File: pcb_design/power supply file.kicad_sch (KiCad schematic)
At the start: 6 parts, among them U3 L78M05CDT, U4 L78M05CDT

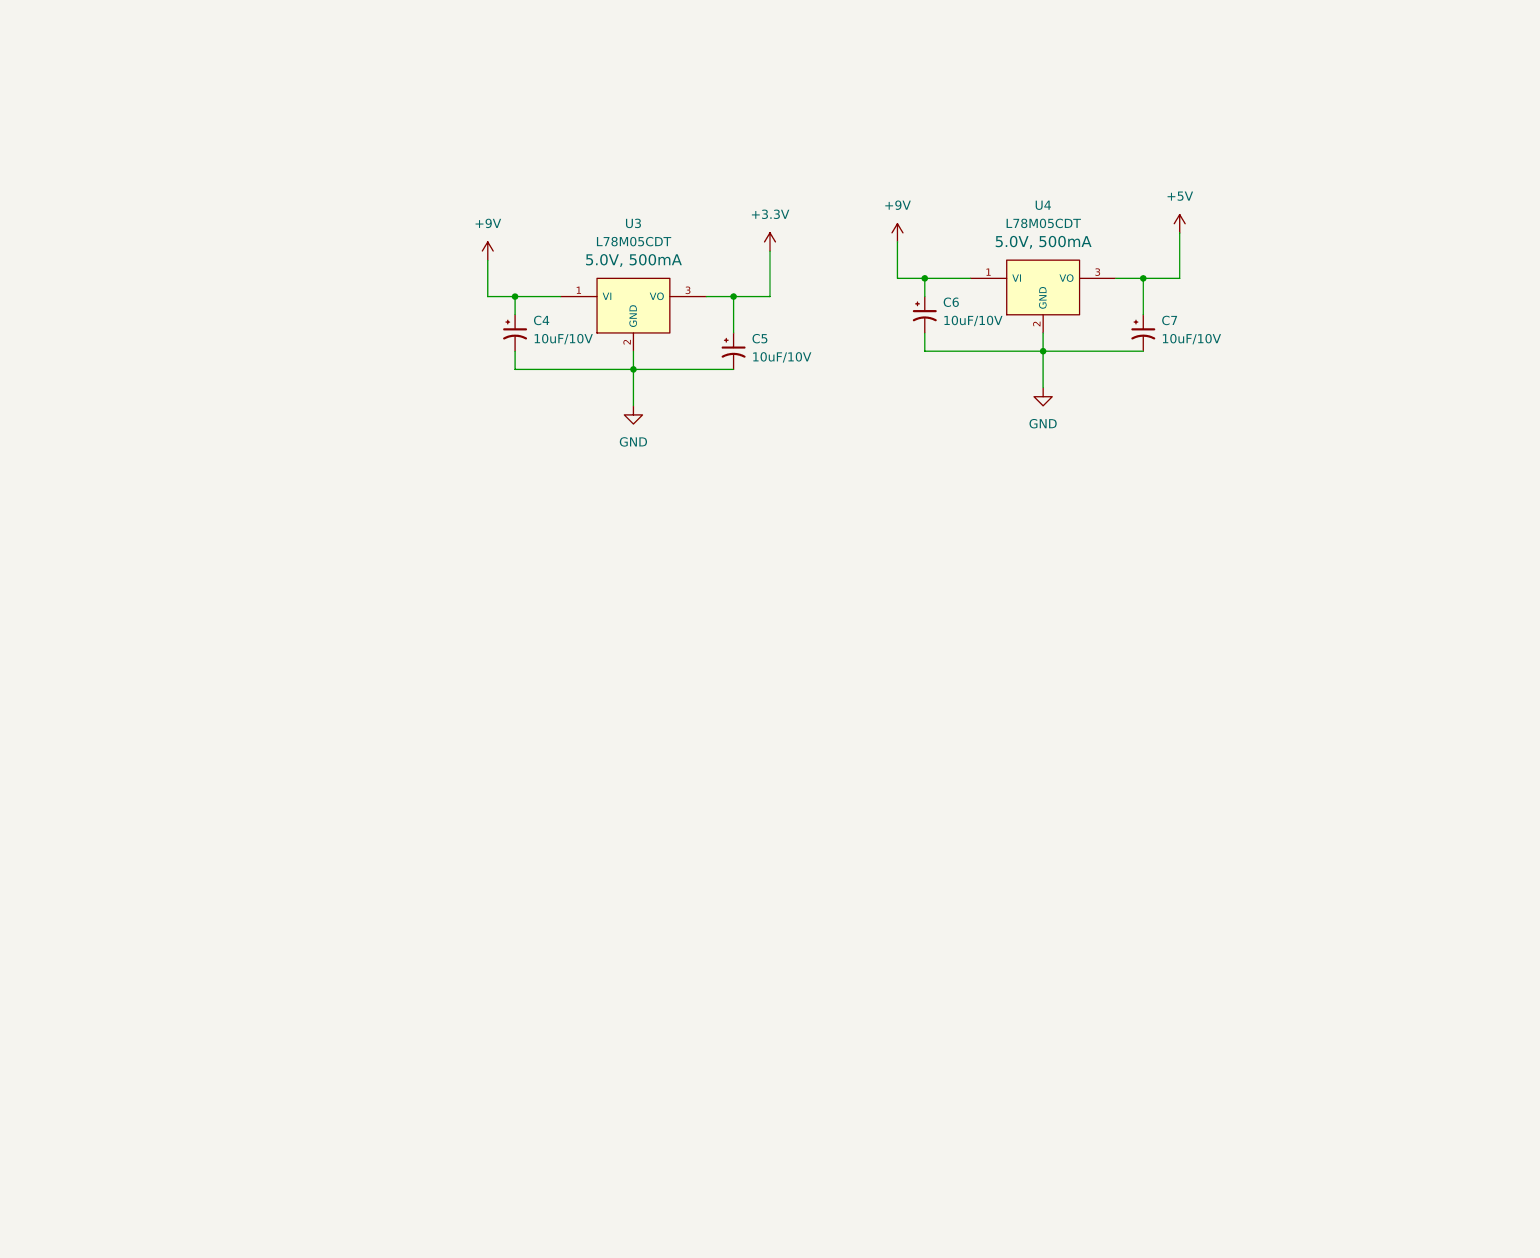
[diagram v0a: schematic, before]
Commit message: cambio de regulador de alto iq por reguladores de bajo iq separados uno para sensores y otro para micro y comunicacion usando el lt8610, apagado de alimentacion de sensores atravez de mosfet canal p
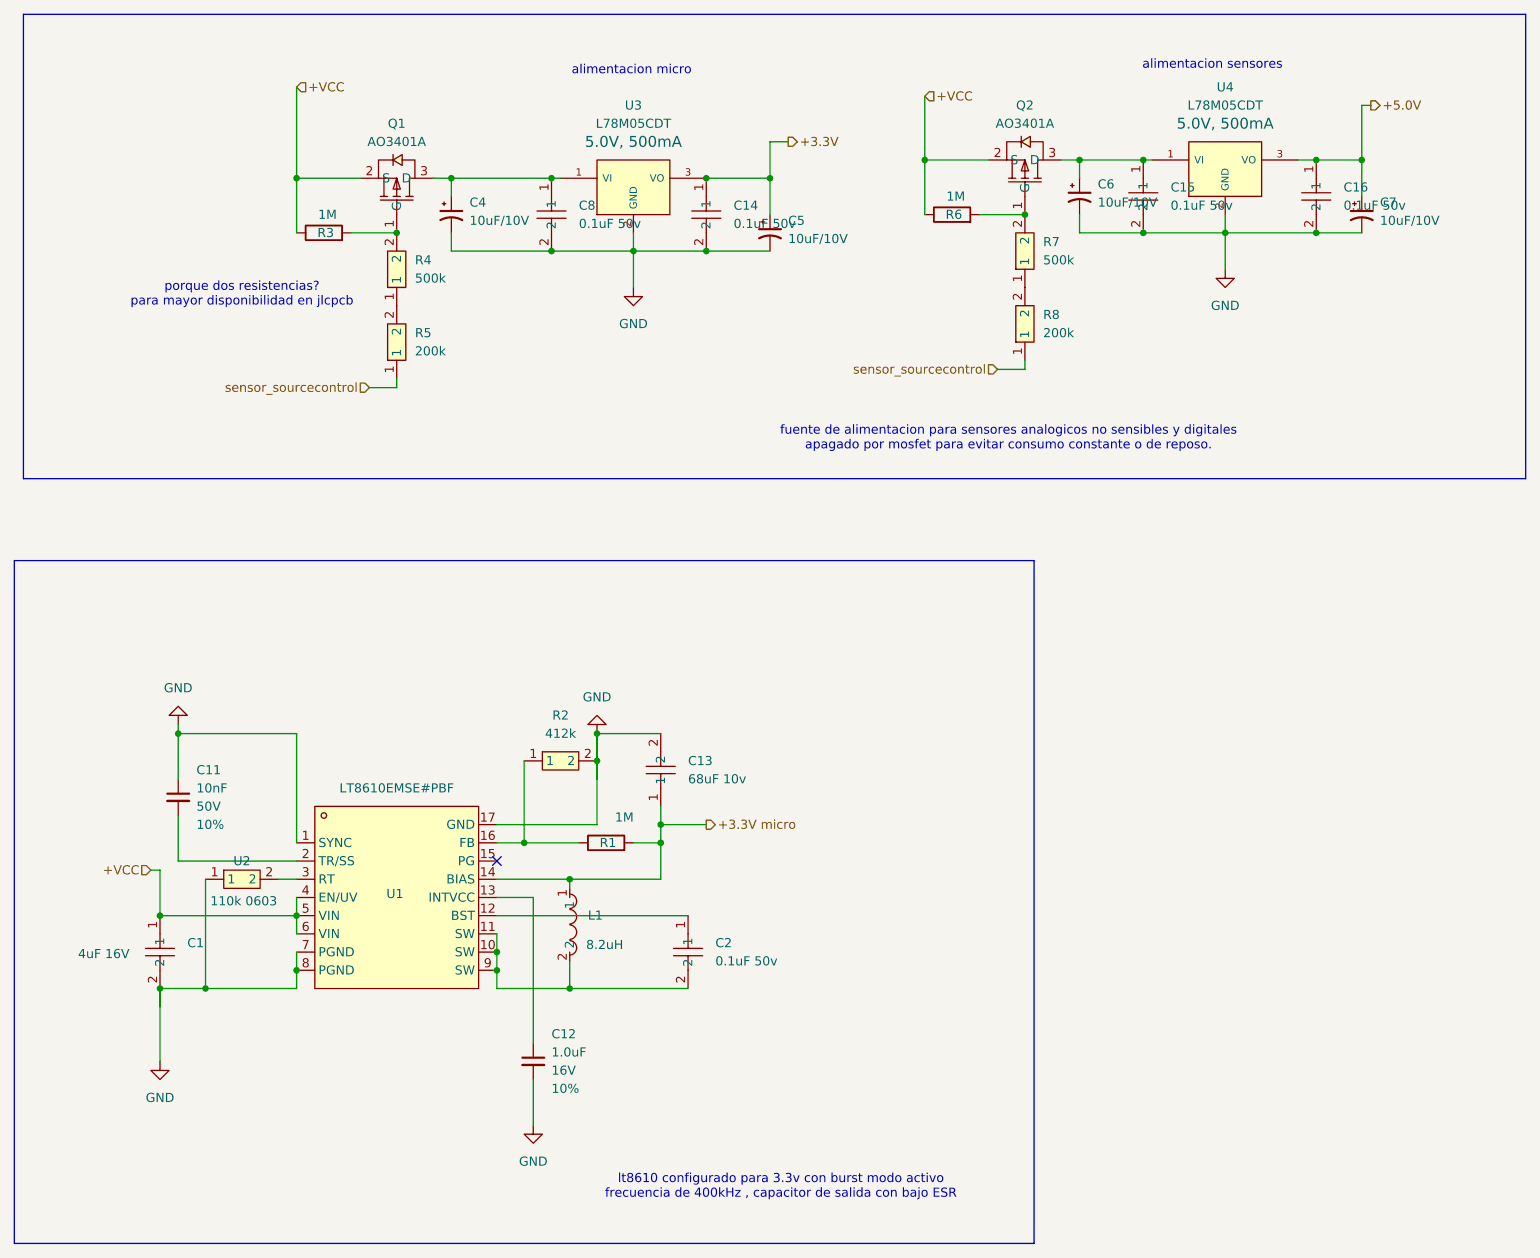
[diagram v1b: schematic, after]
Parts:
- added C1: 4uF 16V, EasyEDA:C0603, symbol EasyEDA:CL10A475KO8NNNC
- added C11: 10nF, PCM_SparkFun-Capacitor:C_0603_1608Metric, symbol PCM_SparkFun-Capacitor:10nF_0603_50V_10%
- added C12: 1.0uF, PCM_SparkFun-Capacitor:C_0603_1608Metric, symbol PCM_SparkFun-Capacitor:1.0uF_0603_16V_10%
- added C13: 68uF 10v, EasyEDA:C1206, symbol EasyEDA:C3216X5R1A686M160AC
- added C14, C15, C16, C2, C8: 0.1uF 50v, EasyEDA:C0603, symbol EasyEDA:CL10B104KB8NNNC
- added L1: 8.2uH, EasyEDA:IND-SMD_L7.0-W6.6_FXL0630, symbol EasyEDA:FXL0630-8R2-M
- added Q1, Q2: AO3401A, EasyEDA:SOT-23_L2.9-W1.3-P1.90-LS2.4-BR, symbol EasyEDA:AO3401A
- added R1, R3, R6: 1M_0603, PCM_4ms_Resistor:R_0603, symbol PCM_4ms_Resistor:1M_0603
- added R2: 412k, EasyEDA:R1206, symbol EasyEDA:RT1206BRD07412KL
- added R4, R7: 500k, EasyEDA:R0805, symbol EasyEDA:ARG05BTC5003
- added R5, R8: 200k, EasyEDA:R0805, symbol EasyEDA:FRC0805F2003TS
- added U1: LT8610EMSE#PBF, EasyEDA:MSOP-16_L4.0-W3.0-P0.50-LS4.9-BL-EP, symbol EasyEDA:LT8610EMSE#PBF
- added U2: 110k 0603, EasyEDA:R0603, symbol EasyEDA:FRC0603F1103TS
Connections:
- net +3.3V: now also C14.1
- net GND: now also C1.2, C11.1, C12.2, C13.2, C14.2, C15.2, C16.2, C8.2, R2.2, U1.1 (SYNC), U1.17 (GND), U1.7 (PGND), U1.8 (PGND), U2.1
- net +5V renamed +5.0V
- net +5.0V: now also C16.1
- net +9V: no longer names the net of C6.1, U4.1 (VI)
- net +9V: now also C15.1, Q2.3 (D); no longer C4.1, U3.1 (VI)
- new net: R1.1, R2.1, U1.16 (FB)
- new net: R4.1, R5.2
- new net: R7.1, R8.2
- new net: Q2.1 (G), R6.2, R7.2
- new net: Q1.1 (G), R3.2, R4.2
- new net: C2.2, L1.2, U1.10 (SW), U1.11 (SW), U1.9 (SW)
- new net: C2.1, U1.12 (BST)
- new net: C12.1, U1.13 (INTVCC)
- new net: C11.2, U1.2 (TR/SS)
- new net: U1.3 (RT), U2.2
- new net: C4.1, C8.1, Q1.3 (D), U3.1 (VI)
- new net +3.3V micro: C13.1, L1.1, R1.2, U1.14 (BIAS)
- new net +VCC: C1.1, Q1.2 (S), Q2.2 (S), R3.1, R6.1, U1.4 (EN/UV), U1.5 (VIN), U1.6 (VIN)
- new net sensor_sourcecontrol: R5.1, R8.1
- no-connect marks 0 -> 1
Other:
- note added: "alimentacion micro"
- note added: "alimentacion sensores"
- note added: "fuente de alimentacion para sensores analogicos no sensibles y digitales apagado por mosfet para evitar consumo constante o de reposo."
- note added: "lt8610 configurado para 3.3v con burst modo activo frecuencia de 400kHz , capacitor de salida con bajo ESR"
- note added: "porque dos resistencias? para mayor disponibilidad en jlcpcb"
- moved on the sheet: C4, C5, C6, C7, U3, U4
